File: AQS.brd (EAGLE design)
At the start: 70 x 60 mm, 40 parts, among them IC1 BME680, IC2 CH340G, IC4 ESPWROOM32, J1 ESP-PROG-2X3-1.27-SHROUDED, J2 M02X5-1.27-S, J3 USB-C-16P-16P, Q1 MMDT3904, Q2 2N7002

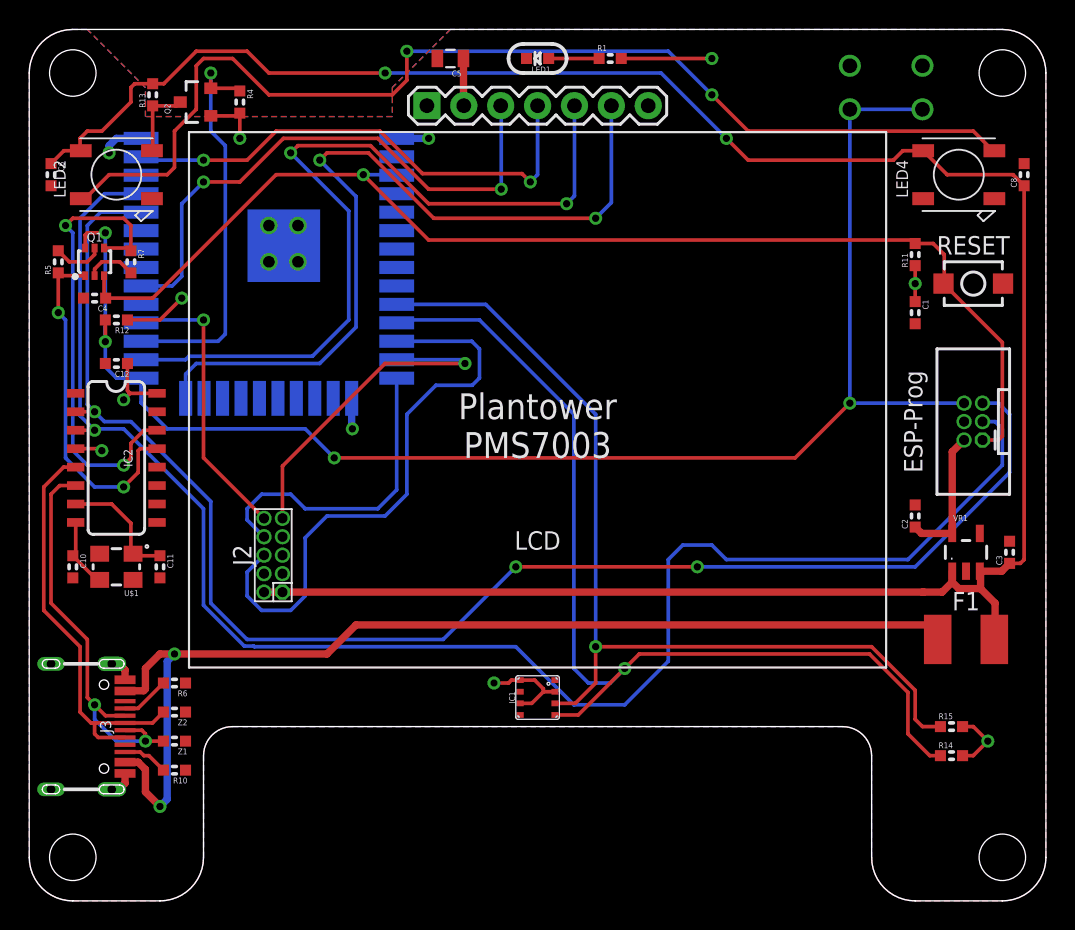
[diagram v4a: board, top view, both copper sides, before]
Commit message: Routing for CP2102N
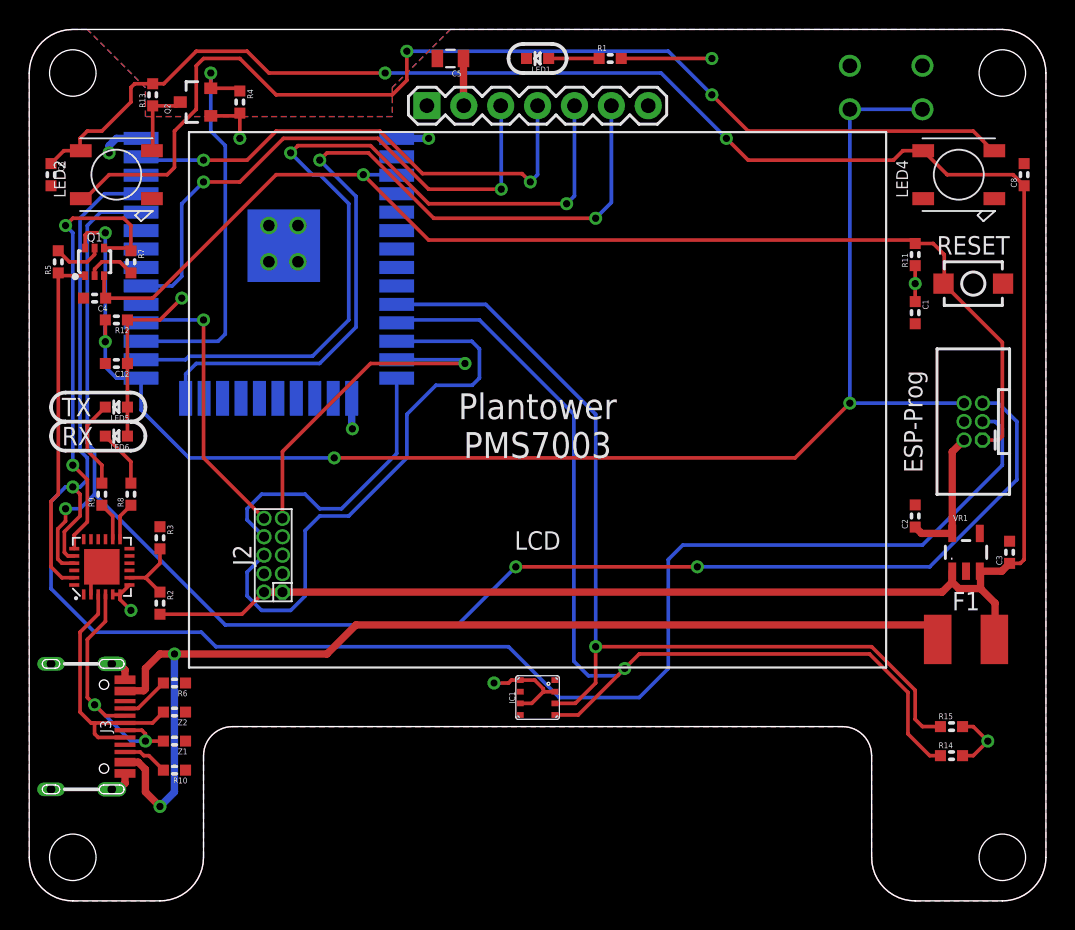
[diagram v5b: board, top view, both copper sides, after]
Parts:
- removed C10, C11: 22pF, SuperHouse-DiscreteSemi:C0603
- removed U$1: 16MHz, SuperHouse-Oscillators:CRYSTAL-SMD-3X2
- added LED5: TX/YEL, SuperHouse-LEDs:LED-0603
- added LED6: RX/GRN, SuperHouse-LEDs:LED-0603
- added R2: 22.1K, SuperHouse-DiscreteSemi:R0603
- added R3: 47.5K, SuperHouse-DiscreteSemi:R0603
- added R8, R9: 1K, SuperHouse-DiscreteSemi:R0603
- IC2: value CH340G -> CP2102N-A01-GQFN24; device SuperHouse-ICs:SO16 -> SuperHouse-ICs:QFN-24
- moved IC2 7.57 mm to (5.00, 24.0), turned to 0 degrees
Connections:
- removed net N$3: C11.1, IC2.7, U$1.1
- new net N$13: LED5.C, R9.2
- new net N$39: IC2.8, R2.1, R3.2
- new net RX_LED: IC2.13, R8.1
- new net TX_LED: IC2.14, R9.1
- net 3.3V: now also IC2.5, IC2.6, IC2.7, LED5.A, LED6.A; no longer IC2.16, IC2.4
- net 5V: now also R2.2
- net D+: now also IC2.3; no longer IC2.5
- net D-: now also IC2.4; no longer IC2.6
- net DTR: now also IC2.23; no longer IC2.13
- net GND: now also IC2.2, IC2.TGND, R3.1; no longer C10.2, C11.2, IC2.1, U$1.2, U$1.4
- net N$2: now also LED6.C, R8.2; no longer C10.1, IC2.8, U$1.3
- net RTS: now also IC2.19; no longer IC2.14
- net RXD0: now also IC2.21; no longer IC2.2
- net TXD0: now also IC2.20; no longer IC2.3
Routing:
- net D+: track 28.6 -> 17.9 mm
- net TXD0: track 111.3 -> 121.9 mm
- net D-: track 28.5 -> 18.5 mm
- net N$3: track 8.42 -> 0.00 mm
- net 5V: track 160.6 -> 168.4 mm
- net N$13: track 0.00 -> 6.17 mm
- net RXD0: track 103.0 -> 108.4 mm
- net N$39: track 0.00 -> 4.91 mm
- net 3.3V: track 47.1 -> 51.4 mm, vias 8 -> 7
- net TX_LED: track 0.00 -> 2.65 mm
- net RX_LED: track 0.00 -> 2.65 mm
- net GND: track 13.8 -> 16.0 mm
- net PMS_RX: track 21.8 -> 20.3 mm
- net PMS_RESET: track 39.8 -> 38.6 mm
- net N$2: track 4.91 -> 3.97 mm
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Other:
- board text added: "RX"
- board text added: "TX"
